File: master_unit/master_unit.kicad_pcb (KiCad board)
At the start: 2 copper layers, 229.9 x 109.2 mm, 12 parts, among them IC1 THVD8000DDFR, J1 Conn_01x03, U1 DEV-15583

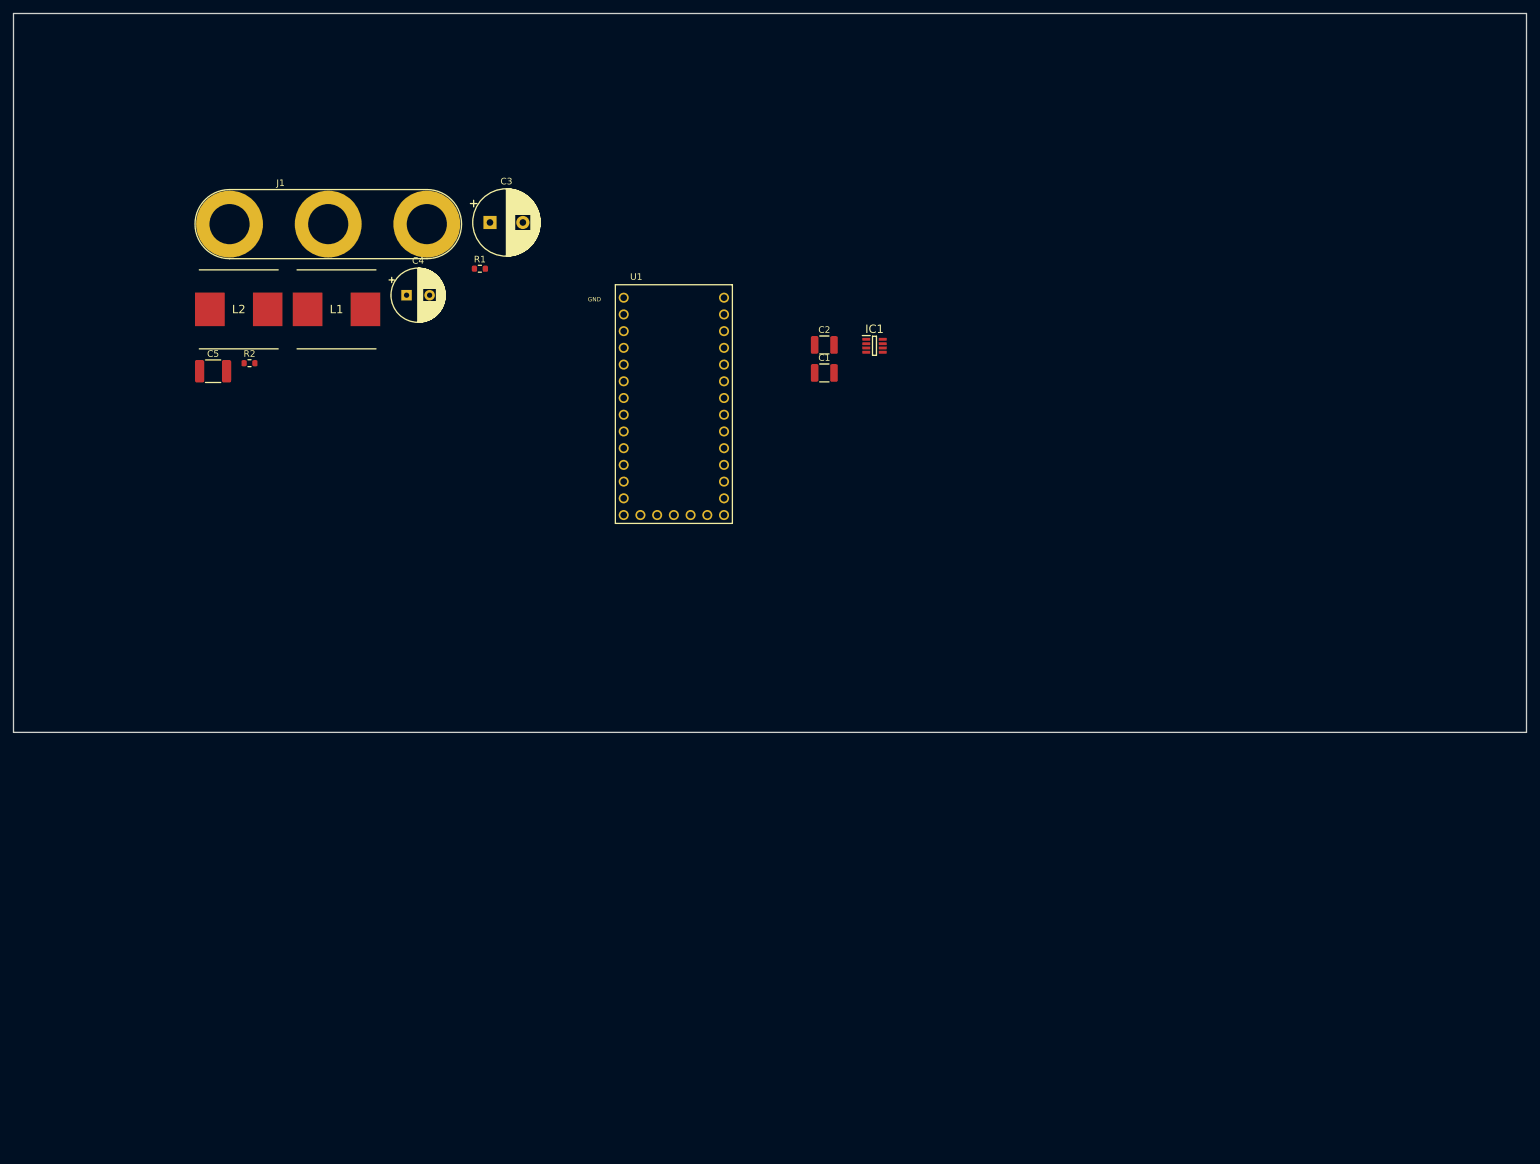
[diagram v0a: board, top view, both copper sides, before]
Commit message: preliminary layout
All basic component are there and a basic layout is performed.
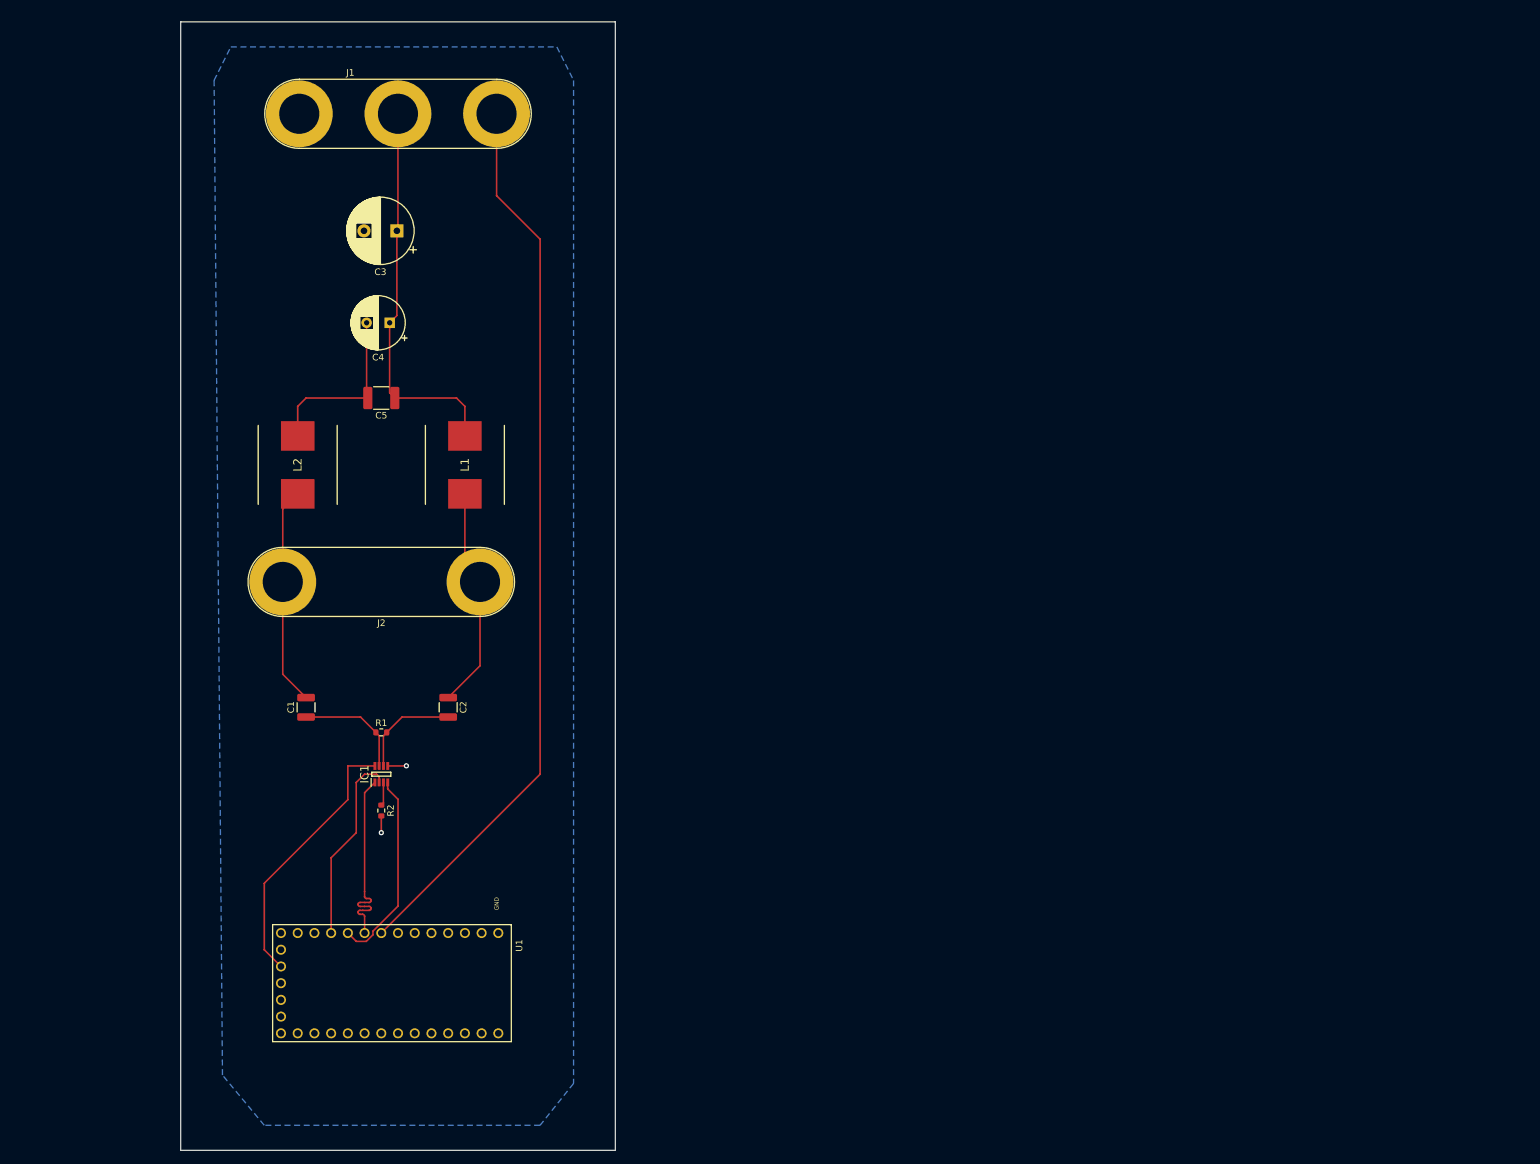
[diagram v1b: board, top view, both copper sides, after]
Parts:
- added J2: Conn_01x02, Connector:Banana_Jack_2Pin, F.Cu at (117.9, 129.5)
- moved IC1 99.2 mm to (102.9, 158.8), turned to 90 degrees
- moved U1 97.7 mm to (104.1, 190.5), turned to -90 degrees
- moved C1 93.7 mm to (91.4, 148.6), turned to 90 degrees
- moved C2 79.4 mm to (113.0, 148.6), turned to -90 degrees
- moved R1 72.0 mm to (102.9, 152.4)
- moved R2 70.9 mm to (102.9, 164.3), turned to -90 degrees
- moved L1 30.6 mm to (115.6, 111.8), turned to -90 degrees
- moved C5 25.9 mm to (102.9, 101.6), turned to 180 degrees
- moved L2 25.3 mm to (90.2, 111.8), turned to -90 degrees
- moved J1 19.8 mm to (90.4, 58.4)
- moved C3 14.2 mm to (105.2, 76.2), turned to 180 degrees
- moved C4 4.92 mm to (104.1, 90.2), turned to 180 degrees
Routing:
- net Trig: track 0.00 -> 137.2 mm
- net Vbb: track 0.00 -> 59.7 mm
- net 3.3V: track 0.00 -> 40.9 mm
- net A: track 0.00 -> 33.9 mm
- net B: track 0.00 -> 33.4 mm
- net GND: track 0.00 -> 32.5 mm, vias 0 -> 2
- net Net-(IC1-Pad4): track 0.00 -> 30.1 mm
- net Net-(IC1-Pad1): track 0.00 -> 30.1 mm
- net MODE: track 0.00 -> 29.5 mm
- net Net-(C1-Pad1): track 0.00 -> 16.9 mm
- net Net-(C2-Pad2): track 0.00 -> 15.6 mm
- net Net-(IC1-Pad3): track 0.00 -> 3.58 mm
- added copper zone on B.Cu, net GND
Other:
- board size 229.9 x 109.2 mm -> 66 x 171.4 mm

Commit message: adjusting layout and trace width
More compact layout
trace width calculation based on a 1A for the Vbb net
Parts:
- moved J1 38.1 mm to (89.1, 96.5)
- moved C5 24.4 mm to (114.3, 80.0)
- moved C4 17.5 mm to (104.1, 72.7), turned to -90 degrees
- moved C3 15.8 mm to (90.2, 71.6), turned to -90 degrees
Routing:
- net Trig: track 137.2 -> 99.6 mm
- net Vbb: track 59.7 -> 69.7 mm
- net GND: track 32.5 -> 26.3 mm
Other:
- board size 66 x 171.4 mm -> 62.2 x 141 mm
- board text added: "A"
- board text added: "B"
- board text added: "GND"
- board text added: "Trig"
- board text added: "Vbb"

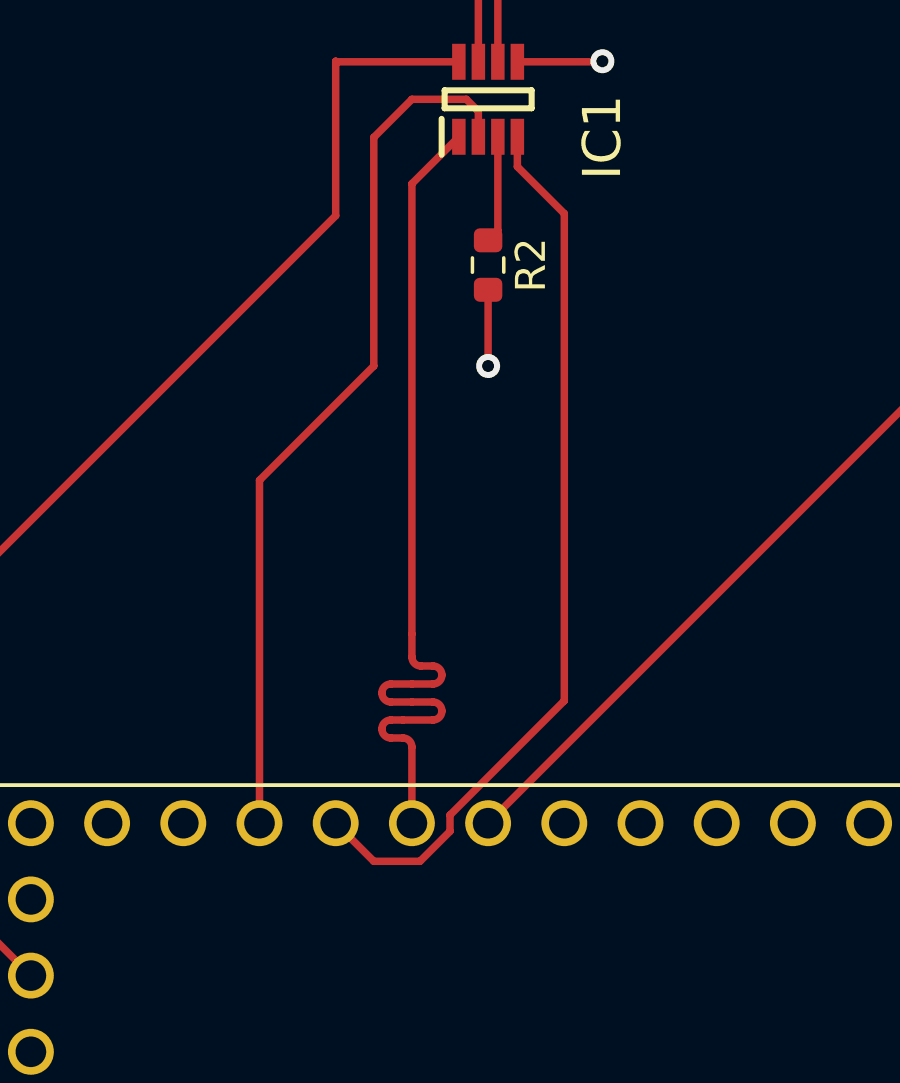
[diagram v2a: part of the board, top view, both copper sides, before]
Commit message: pushing workerBoard in kicad version
Still some bugs:
- Pad 4 and 8 of the op amp are not connected to the good net
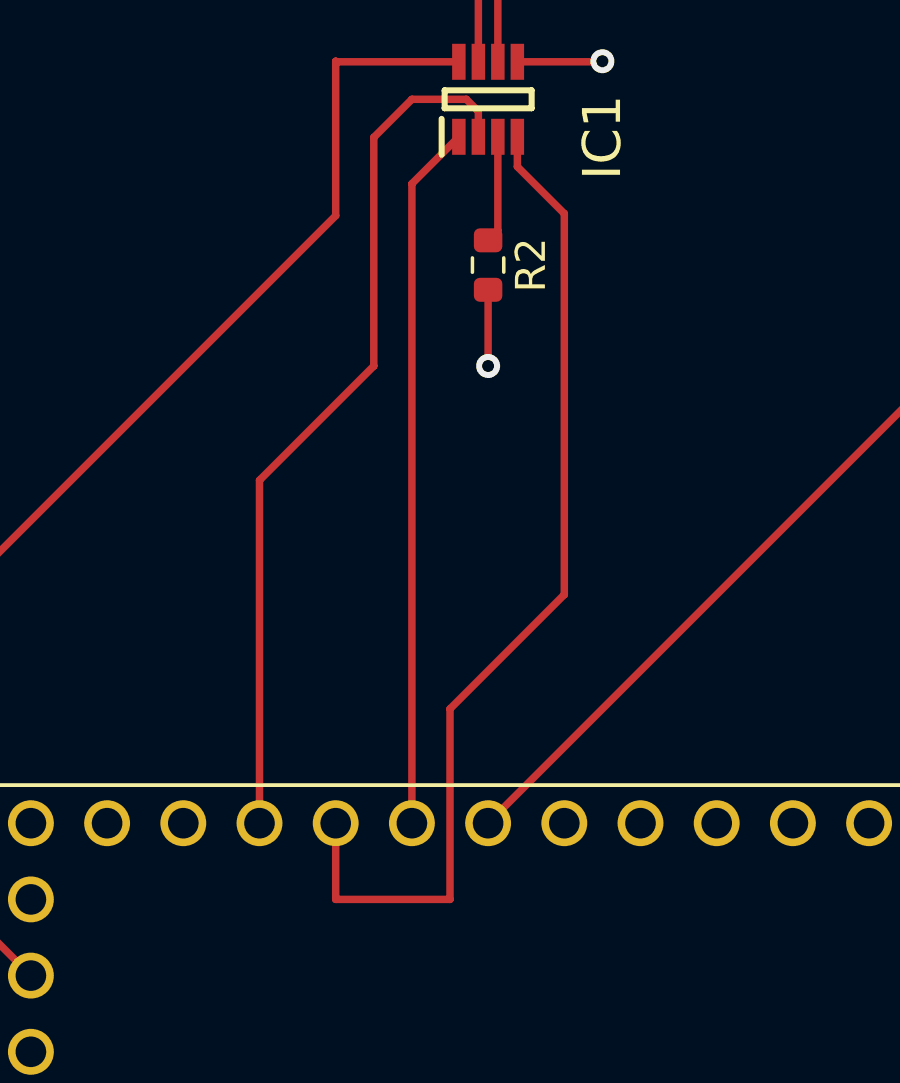
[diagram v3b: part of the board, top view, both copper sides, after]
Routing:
- net Net-(IC1-Pad1): track 30.1 -> 23.5 mm
- net Net-(IC1-Pad4): track 30.1 -> 34.0 mm
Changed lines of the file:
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@@
   (via (at 102.87 167.64) (size 0.8) (drill 0.4) (layers "F.Cu" "B.Cu") (free) (net 25))
   (via (at 106.68 157.48) (size 0.8) (drill 0.4) (layers "F.Cu" "B.Cu") (free) (net 25))
-  (segment (start 100.33 182.88) (end 100.33 180.34) (width 0.25) (layer "F.Cu") (net 26))
-  (segment (start 101.03 177.64) (end 100.63 177.64) (width 0.25) (layer "F.Cu") (net 26))
-  (segment (start 99.63 179.44) (end 100.03 179.44) (width 0.25) (layer "F.Cu") (net 26))
   (segment (start 100.33 161.565) (end 101.895 160) (width 0.25) (layer "F.Cu") (net 26))
-  (segment (start 100.33 177.34) (end 100.33 176.573423) (width 0.25) (layer "F.Cu") (net 26))
-  (segment (start 100.33 178.84) (end 99.63 178.84) (width 0.25) (layer "F.Cu") (net 26))
-  (segment (start 100.03 179.44) (end 101.03 179.44) (width 0.25) (layer "F.Cu") (net 26))
-  (segment (start 101.03 178.84) (end 100.33 178.84) (width 0.25) (layer "F.Cu") (net 26))
-  (segment (start 100.33 178.24) (end 101.03 178.24) (width 0.25) (layer "F.Cu") (net 26))
-  (segment (start 100.33 176.573423) (end 100.33 161.565) (width 0.25) (layer "F.Cu") (net 26))
-  (segment (start 100.03 180.04) (end 99.63 180.04) (width 0.25) (layer "F.Cu") (net 26))
-  (segment (start 99.63 178.24) (end 100.33 178.24) (width 0.25) (layer "F.Cu") (net 26))
-  (arc (start 101.33 177.94) (mid 101.242132 177.727868) (end 101.03 177.64) (width 0.25) (layer "F.Cu") (net 26))
-  (arc (start 99.63 178.84) (mid 99.417868 178.752132) (end 99.33 178.54) (width 0.25) (layer "F.Cu") (net 26))
-  (arc (start 99.33 178.54) (mid 99.417868 178.327868) (end 99.63 178.24) (width 0.25) (layer "F.Cu") (net 26))
-  (arc (start 101.03 178.24) (mid 101.242132 178.152132) (end 101.33 177.94) (width 0.25) (layer "F.Cu") (net 26))
-  (arc (start 100.63 177.64) (mid 100.417868 177.552132) (end 100.33 177.34) (width 0.25) (layer "F.Cu") (net 26))
-  (arc (start 101.33 179.14) (mid 101.242132 178.927868) (end 101.03 178.84) (width 0.25) (layer "F.Cu") (net 26))
-  (arc (start 99.33 179.74) (mid 99.417868 179.527868) (end 99.63 179.44) (width 0.25) (layer "F.Cu") (net 26))
-  (arc (start 101.03 179.44) (mid 101.242132 179.352132) (end 101.33 179.14) (width 0.25) (layer "F.Cu") (net 26))
-  (arc (start 99.63 180.04) (mid 99.417868 179.952132) (end 99.33 179.74) (width 0.25) (layer "F.Cu") (net 26))
-  (arc (start 100.33 180.34) (mid 100.242132 180.127868) (end 100.03 180.04) (width 0.25) (layer "F.Cu") (net 26))
+  (segment (start 100.33 161.565) (end 100.33 182.88) (width 0.25) (layer "F.Cu") (net 26))
   (segment (start 99.06 160.02) (end 99.06 167.64) (width 0.25) (layer "F.Cu") (net 27))
   (segment (start 102.545 159.15) (end 102.145 158.75) (width 0.25) (layer "F.Cu") (net 27))
@@
   (segment (start 103.195 160) (end 103.195 163.125) (width 0.25) (layer "F.Cu") (net 31))
   (segment (start 103.195 163.125) (end 102.87 163.45) (width 0.25) (layer "F.Cu") (net 31))
-  (segment (start 100.600802 184.15) (end 101.6 183.150802) (width 0.25) (layer "F.Cu") (net 32))
-  (segment (start 99.06 184.15) (end 100.600802 184.15) (width 0.25) (layer "F.Cu") (net 32))
-  (segment (start 101.6 183.150802) (end 101.6 182.609198) (width 0.25) (layer "F.Cu") (net 32))
-  (segment (start 105.41 178.799198) (end 105.41 162.56) (width 0.25) (layer "F.Cu") (net 32))
-  (segment (start 101.6 182.609198) (end 105.41 178.799198) (width 0.25) (layer "F.Cu") (net 32))
+  (segment (start 105.41 175.26) (end 101.6 179.07) (width 0.25) (layer "F.Cu") (net 32))
+  (segment (start 105.41 162.56) (end 105.41 175.26) (width 0.25) (layer "F.Cu") (net 32))
   (segment (start 105.41 162.56) (end 103.845 160.995) (width 0.25) (layer "F.Cu") (net 32))
-  (segment (start 97.79 182.88) (end 99.06 184.15) (width 0.25) (layer "F.Cu") (net 32))
+  (segment (start 101.6 179.07) (end 101.6 185.42) (width 0.25) (layer "F.Cu") (net 32))
+  (segment (start 97.79 185.42) (end 97.79 182.88) (width 0.25) (layer "F.Cu") (net 32))
   (segment (start 103.845 160.995) (end 103.845 160) (width 0.25) (layer "F.Cu") (net 32))
+  (segment (start 101.6 185.42) (end 97.79 185.42) (width 0.25) (layer "F.Cu") (net 32))
   (segment (start 85.09 175.33) (end 97.79 162.63) (width 0.25) (layer "F.Cu") (net 33))
   (segment (start 87.63 187.96) (end 85.09 185.42) (width 0.25) (layer "F.Cu") (net 33))
